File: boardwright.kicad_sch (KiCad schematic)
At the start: 0 parts

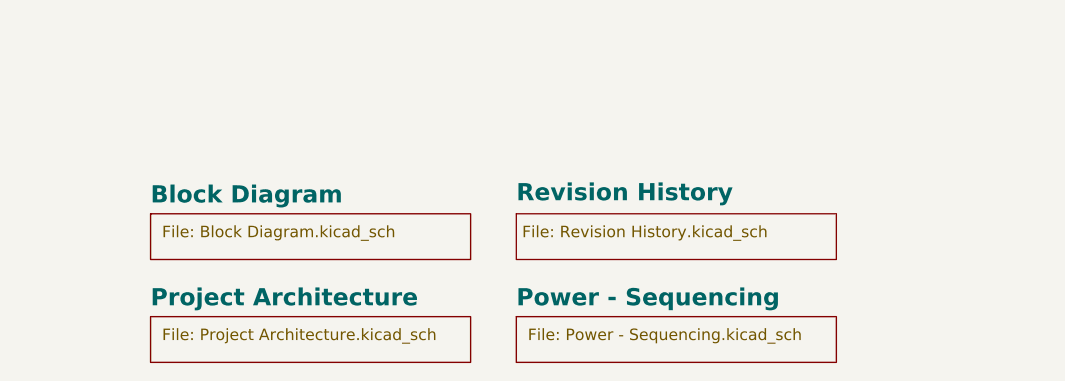
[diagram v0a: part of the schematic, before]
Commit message: feat: convert template to Boardwright
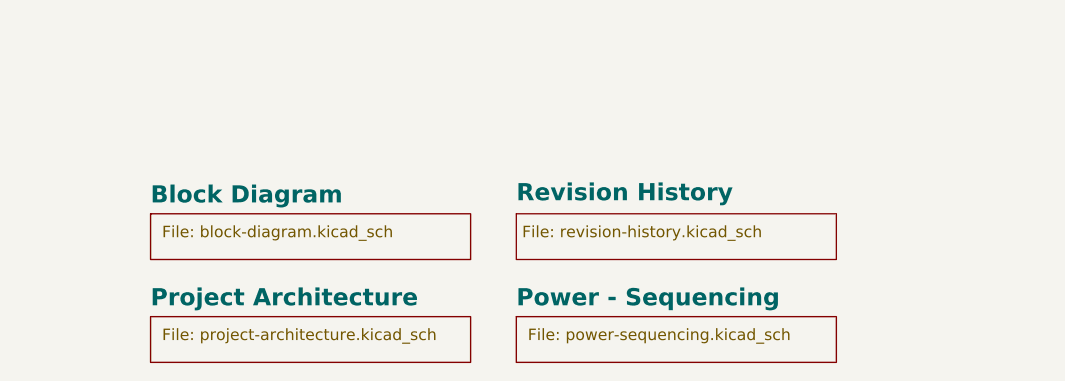
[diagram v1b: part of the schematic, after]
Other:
- sheet Block Diagram: file Block Diagram.kicad_sch -> block-diagram.kicad_sch
- sheet Power - Sequencing: file Power - Sequencing.kicad_sch -> power-sequencing.kicad_sch
- sheet Project Architecture: file Project Architecture.kicad_sch -> project-architecture.kicad_sch
- sheet Revision History: file Revision History.kicad_sch -> revision-history.kicad_sch
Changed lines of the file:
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@@
 			)
 		)
-		(property "Sheetfile" "Power - Sequencing.kicad_sch"
+		(property "Sheetfile" "power-sequencing.kicad_sch"
 			(at 341.63 314.96 0)
 			(effects
@@
 		)
 		(instances
-			(project "KDT_Hierarchical_KiBot"
+			(project "boardwright"
 				(path "/f9e05184-c88b-4a88-ae9c-ab2bdb32be7c"
 					(page "6")
@@
 			)
 		)
-		(property "Sheetfile" "Revision History.kicad_sch"
+		(property "Sheetfile" "revision-history.kicad_sch"
 			(at 340.995 303.53 0)
 			(effects
@@
 		)
 		(instances
-			(project "KDT_Hierarchical_KiBot"
+			(project "boardwright"
 				(path "/f9e05184-c88b-4a88-ae9c-ab2bdb32be7c"
 					(page "7")
@@
 			)
 		)
-		(property "Sheetfile" "Block Diagram.kicad_sch"
+		(property "Sheetfile" "block-diagram.kicad_sch"
 			(at 300.99 303.53 0)
 			(effects
@@
 		)
 		(instances
-			(project "KDT_Hierarchical_KiBot"
+			(project "boardwright"
 				(path "/f9e05184-c88b-4a88-ae9c-ab2bdb32be7c"
 					(page "2")
@@
 			)
 		)
-		(property "Sheetfile" "Project Architecture.kicad_sch"
+		(property "Sheetfile" "project-architecture.kicad_sch"
 			(at 300.99 314.96 0)
 			(effects
@@
 		)
 		(instances
-			(project "KDT_Hierarchical_KiBot"
+			(project "boardwright"
 				(path "/f9e05184-c88b-4a88-ae9c-ab2bdb32be7c"
 					(page "3")

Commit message: feat: prepare Boardwright template workflow
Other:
- sheet Block Diagram renamed BLOCK DIAGRAM
- sheet Power - Sequencing renamed POWER SEQUENCE
- sheet Project Architecture renamed PROJECT
- sheet Revision History renamed REVISION HISTORY
- sheet POWER SEQUENCE: file power-sequencing.kicad_sch -> power-sequence.kicad_sch
- sheet PROJECT: file project-architecture.kicad_sch -> project.kicad_sch
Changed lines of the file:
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@@
 			(color 0 0 0 0.0000)
 		)
-		(property "Sheetname" "Power - Sequencing"
+		(property "Sheetname" "POWER SEQUENCE"
 			(at 340.36 312.6609 0)
 			(effects
@@
 			)
 		)
-		(property "Sheetfile" "power-sequencing.kicad_sch"
+		(property "Sheetfile" "power-sequence.kicad_sch"
 			(at 341.63 314.96 0)
 			(effects
@@
 			(color 0 0 0 0.0000)
 		)
-		(property "Sheetname" "Revision History"
+		(property "Sheetname" "REVISION HISTORY"
 			(at 340.36 300.99 0)
 			(effects
@@
 			(color 0 0 0 0.0000)
 		)
-		(property "Sheetname" "Block Diagram"
+		(property "Sheetname" "BLOCK DIAGRAM"
 			(at 299.72 301.2309 0)
 			(effects
@@
 			(color 0 0 0 0.0000)
 		)
-		(property "Sheetname" "Project Architecture"
+		(property "Sheetname" "PROJECT"
 			(at 299.72 312.6609 0)
 			(effects
@@
 			)
 		)
-		(property "Sheetfile" "project-architecture.kicad_sch"
+		(property "Sheetfile" "project.kicad_sch"
 			(at 300.99 314.96 0)
 			(effects
